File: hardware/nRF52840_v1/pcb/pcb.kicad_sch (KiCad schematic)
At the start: 151 parts, among them SW1 SW_DIP_x01, Y1 32.768 kHz

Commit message: M  hardware/nRF52840_v1/border.py M  hardware/nRF52840_v1/pcb/pcb.kicad_pcb M  hardware/nRF52840_v1/pcb/pcb.kicad_prl M  hardware/nRF52840_v1/pcb/pcb.kicad_pro M  hardware/nRF52840_v1/pcb/pcb.kicad_sch M  hardware/nRF52840_v1/pcb/switch.kicad_sch A  hardware/nRF52840_v1/pcb/usbcover/usbcover.kicad_pcb A  hardware/nRF52840_v1/pcb/usbcover/usbcover.kicad_prl A  hardware/nRF52840_v1/pcb/usbcover/usbcover.kicad_pro A  hardware/nRF52840_v1/pcb/usbcover/usbcover.kicad_sch M  hardware/nRF52840_v1/placefp.py A  hardware/nRF52840_v1/tmr-footprints/Aliexpress_SW_DIP_3.6x7.3mm.kicad_mod A  hardware/nRF52840_v1/tmr-footprints/Aliexpress_SW_DIP_TS_1136W_3x6x5mm.kicad_mod A  hardware/nRF52840_v1/tmr-footprints/SAMTEC-FTSH-105-01-X-D-RA.kicad_mod A  hardware/nRF52840_v1/tmr-footprints/SAMTEC-FTSH-105-01-X-DH.kicad_mod A  hardware/nRF52840_v1/tmr-footprints/SAMTEC-FTSH-105-01-X-DV.kicad_mod D  hardware/nRF52840_v1/tmr-footprints/sw_lowpro_combo_MDT.kicad_mod D  hardware/nRF52840_v1/tmr-footprints/sw_lowpro_gateron_MDT.kicad_mod M  hardware/nRF52840_v1/tmr-symbols.kicad_sym M  hardware/nRF52840_v2/pcb/pcb.kicad_prl M  hardware/nRF54L15_v1/placefp.py
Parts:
- removed JTAG2: Conn_ARM_JTAG_SWD_10, Connector:Tag-Connect_TC2050-IDC-NL_2x05_P1.27mm_Vertical, symbol Connector:Conn_ARM_JTAG_SWD_10
- JTAG1: footprint tmr-lib:SAMTEC-CLP-105-02-X-D-A -> tmr-lib:SAMTEC-FTSH-105-01-X-DV
- SW1: footprint tmr-lib:Button_Switch_3x4x2.5 -> tmr-lib:Aliexpress_SW_DIP_TS_1136W_3x6x5mm
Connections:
- no-connect marks 40 -> 38

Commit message: M  hardware/nRF52840_v1/border.py M  hardware/nRF52840_v1/pcb/pcb.kicad_pcb M  hardware/nRF52840_v1/pcb/pcb.kicad_prl M  hardware/nRF52840_v1/pcb/pcb.kicad_sch M  hardware/nRF52840_v1/pcb/switch.kicad_sch M  hardware/nRF52840_v1/placefp.py A  hardware/nRF52840_v1/tmr-footprints/Aliexpress_SW_DIP_TS_1292V_4x6.2x1.8mm.kicad_mod D  hardware/nRF52840_v1/tmr-footprints/SAMTEC-CLP-105-02-X-D-A-altium.kicad_mod M  hardware/nRF52840_v1/tmr-footprints/SAMTEC-CLP-105-02-X-D-A.kicad_mod
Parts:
- added SW1: SW_DIP_x01, tmr-lib:Aliexpress_SW_DIP_TS_1292V_4x6.2x1.8mm, symbol Switch:SW_DIP_x01
- JTAG1: footprint tmr-lib:SAMTEC-FTSH-105-01-X-DV -> tmr-lib:SAMTEC-CLP-105-02-X-D-A
- SW2: renamed from SW1; footprint tmr-lib:Aliexpress_SW_DIP_TS_1136W_3x6x5mm -> tmr-lib:Aliexpress_SW_DIP_TS_1292V_4x6.2x1.8mm
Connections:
- net GND: now also SW1.1
- net NRESET: now also SW1.2

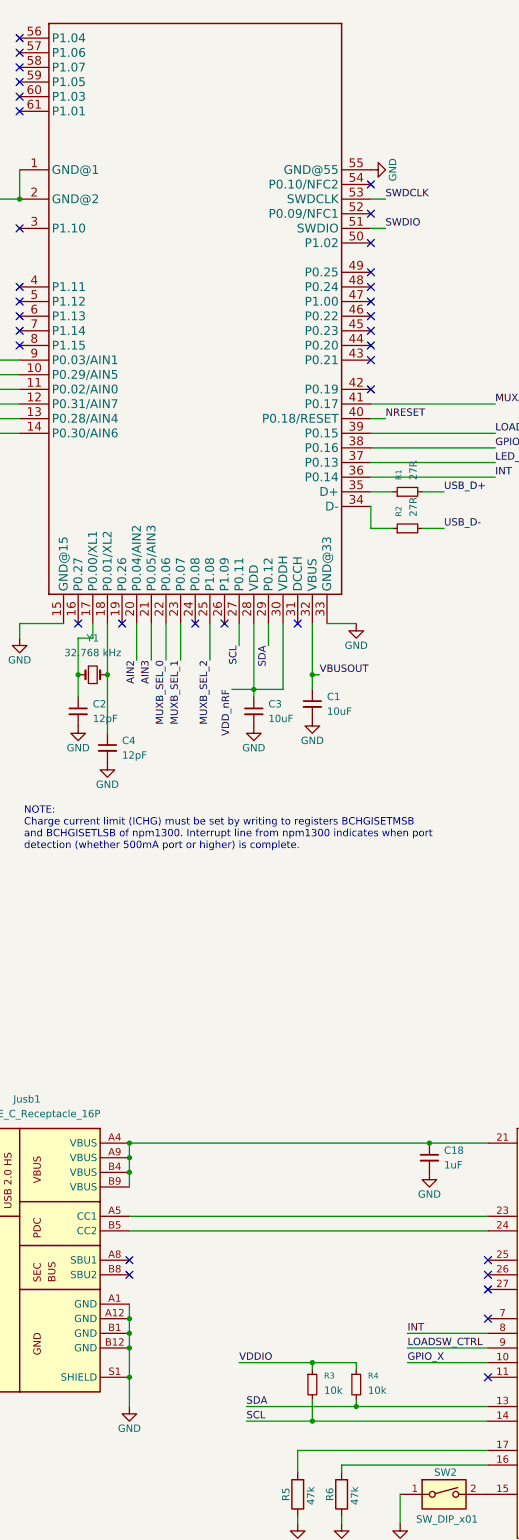
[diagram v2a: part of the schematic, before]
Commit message: M  hardware/nRF52840_v1/border.py M  hardware/nRF52840_v1/pcb/pcb.kicad_pcb M  hardware/nRF52840_v1/pcb/pcb.kicad_prl M  hardware/nRF52840_v1/pcb/pcb.kicad_sch M  hardware/nRF52840_v1/placefp.py A  hardware/nRF52840_v1/tmr-footprints/GCT_USB4215-03-A_REVA.kicad_mod A  hardware/nRF52840_v1/tmr-footprints/LP5864-VQFN-32-1EP_4x4mm_P0.4mm_EP2.8x2.8mm_ThermalVias.kicad_mod
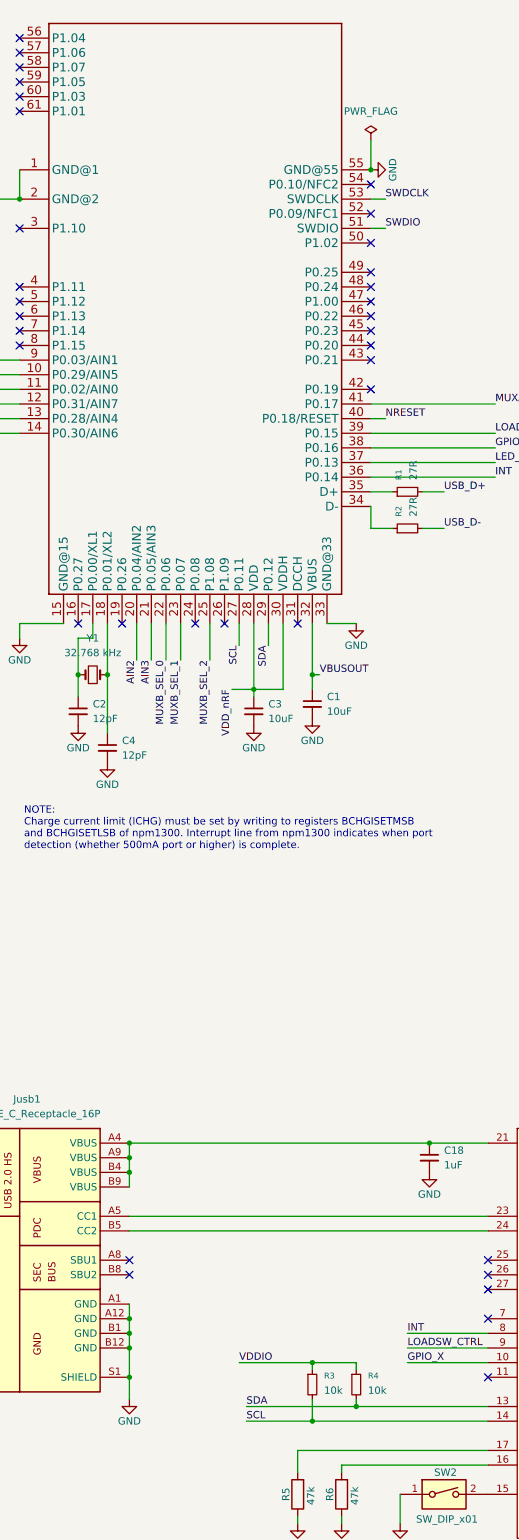
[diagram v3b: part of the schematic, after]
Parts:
- Jusb1: footprint Connector_USB:USB_C_Receptacle_XKB_U262-16XN-4BVC11 -> tmr-lib:GCT_USB4215-03-A_REVA
- LEDDR1: footprint Package_DFN_QFN:VQFN-32-1EP_4x4mm_P0.4mm_EP2.8x2.8mm_ThermalVias -> tmr-lib:LP5864-VQFN-32-1EP_4x4mm_P0.4mm_EP2.8x2.8mm_ThermalVias
